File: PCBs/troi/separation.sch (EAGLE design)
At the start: 2 parts

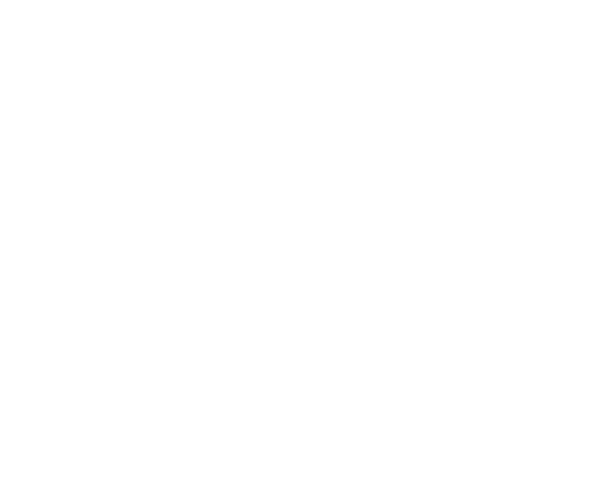
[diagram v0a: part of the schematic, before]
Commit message: added servo connection
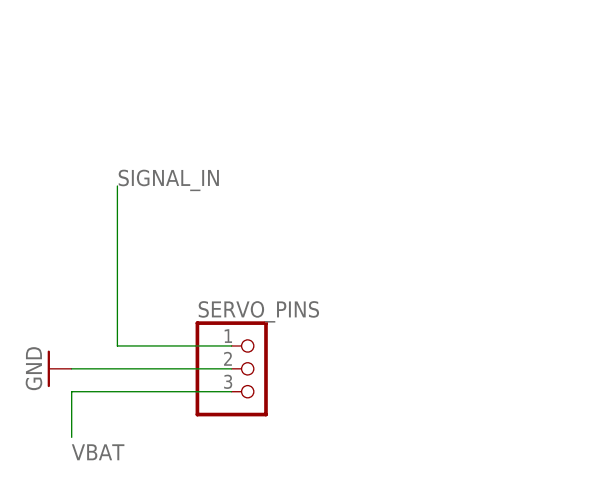
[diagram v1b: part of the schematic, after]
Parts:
- added SERVO_PINS: (no value), pinhead:PINHD-1X3
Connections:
- new net SIGNAL_IN: SERVO_PINS.1
- new net VBAT: SERVO_PINS.3
- net GND: now also SERVO_PINS.2
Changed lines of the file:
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@@
 <part name="+3V1" library="supply1" library_urn="urn:adsk.eagle:library:371" deviceset="+3V3" device=""/>
 <part name="GND1" library="supply1" library_urn="urn:adsk.eagle:library:371" deviceset="GND" device=""/>
+<part name="SERVO_PINS" library="pinhead" library_urn="urn:adsk.eagle:library:325" deviceset="PINHD-1X3" device="" package3d_urn="urn:adsk.eagle:package:22458/2"/>
+<part name="GND2" library="supply1" library_urn="urn:adsk.eagle:library:371" deviceset="GND" device=""/>
 </parts>
 <sheets>
@@
 <instance part="GND1" gate="1" x="93.98" y="86.36" smashed="yes" rot="R270">
 <attribute name="VALUE" x="86.36" y="86.36" size="1.778" layer="96"/>
+</instance>
+<instance part="SERVO_PINS" gate="A" x="30.48" y="53.34" smashed="yes">
+<attribute name="NAME" x="24.13" y="59.055" size="1.778" layer="95"/>
+<attribute name="VALUE" x="24.13" y="45.72" size="1.778" layer="96"/>
+</instance>
+<instance part="GND2" gate="1" x="7.62" y="53.34" smashed="yes" rot="R270">
+<attribute name="VALUE" x="5.08" y="55.88" size="1.778" layer="96" rot="R270"/>
 </instance>
 </instances>
@@
 <pinref part="GND1" gate="1" pin="GND"/>
 </segment>
+<segment>
+<pinref part="SERVO_PINS" gate="A" pin="2"/>
+<wire x1="27.94" y1="53.34" x2="10.16" y2="53.34" width="0.1524" layer="91"/>
+<pinref part="GND2" gate="1" pin="GND"/>
+</segment>
 </net>
 <net name="+3V3" class="0">
@@
 </segment>
 </net>
+<net name="SIGNAL_IN" class="0">
+<segment>
+<pinref part="SERVO_PINS" gate="A" pin="1"/>
+<wire x1="27.94" y1="55.88" x2="15.24" y2="55.88" width="0.1524" layer="91"/>
+<wire x1="15.24" y1="55.88" x2="15.24" y2="73.66" width="0.1524" layer="91"/>
+<label x="15.24" y="73.66" size="1.778" layer="95"/>
+</segment>
+</net>
+<net name="VBAT" class="0">
+<segment>
+<pinref part="SERVO_PINS" gate="A" pin="3"/>
+<wire x1="27.94" y1="50.8" x2="10.16" y2="50.8" width="0.1524" layer="91"/>
+<wire x1="10.16" y1="50.8" x2="10.16" y2="45.72" width="0.1524" layer="91"/>
+<label x="10.16" y="43.18" size="1.778" layer="95"/>
+</segment>
+</net>

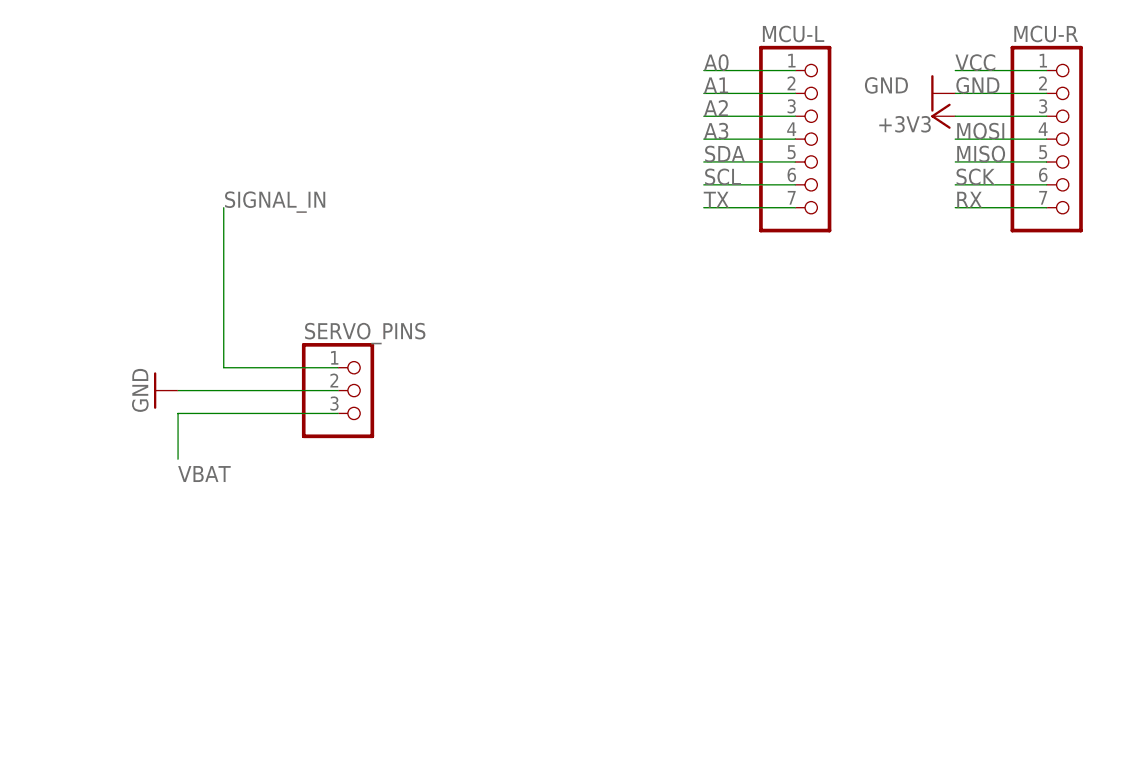
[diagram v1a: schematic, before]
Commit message: added battery terminal
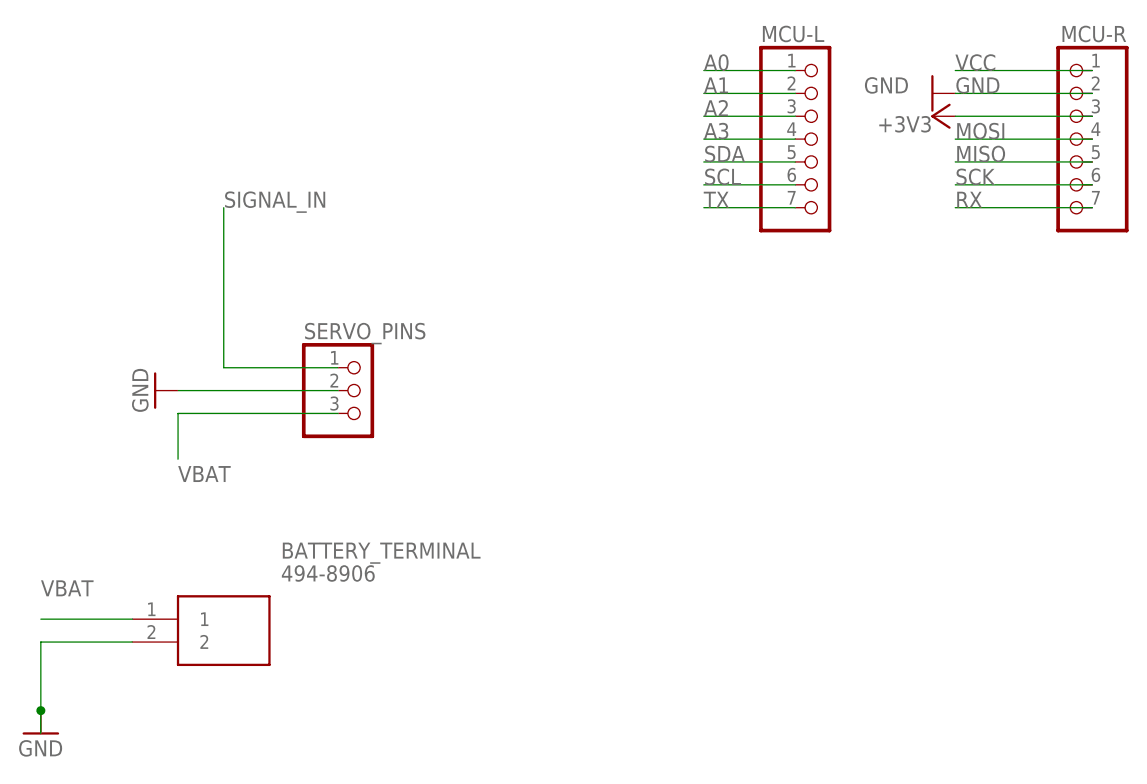
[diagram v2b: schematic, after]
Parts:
- added BATTERY_TERMINAL: 494-8906, 494-8906:494-8906
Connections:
- net GND: now also BATTERY_TERMINAL.2
- net VBAT: now also BATTERY_TERMINAL.1
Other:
- moved on the sheet: MCU-R
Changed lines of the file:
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@@
 <part name="SERVO_PINS" library="pinhead" library_urn="urn:adsk.eagle:library:325" deviceset="PINHD-1X3" device="" package3d_urn="urn:adsk.eagle:package:22458/2"/>
 <part name="GND2" library="supply1" library_urn="urn:adsk.eagle:library:371" deviceset="GND" device=""/>
+<part name="BATTERY_TERMINAL" library="494-8906" deviceset="494-8906" device=""/>
+<part name="GND3" library="supply1" library_urn="urn:adsk.eagle:library:371" deviceset="GND" device=""/>
 </parts>
 <sheets>
@@
 <attribute name="VALUE" x="74.93" y="68.58" size="1.778" layer="96"/>
 </instance>
-<instance part="MCU-R" gate="A" x="109.22" y="81.28" smashed="yes">
-<attribute name="NAME" x="102.87" y="92.075" size="1.778" layer="95"/>
-<attribute name="VALUE" x="102.87" y="68.58" size="1.778" layer="96"/>
+<instance part="MCU-R" gate="A" x="109.22" y="81.28" smashed="yes" rot="MR0">
+<attribute name="NAME" x="115.57" y="92.075" size="1.778" layer="95" rot="MR0"/>
+<attribute name="VALUE" x="115.57" y="68.58" size="1.778" layer="96" rot="MR0"/>
 </instance>
 <instance part="+3V1" gate="G$1" x="93.98" y="83.82" smashed="yes" rot="R90">
@@
 <instance part="GND2" gate="1" x="7.62" y="53.34" smashed="yes" rot="R270">
 <attribute name="VALUE" x="5.08" y="55.88" size="1.778" layer="96" rot="R270"/>
+</instance>
+<instance part="BATTERY_TERMINAL" gate="G$1" x="5.08" y="27.94" smashed="yes">
+<attribute name="NAME" x="21.59" y="35.56" size="1.778" layer="95" align="center-left"/>
+<attribute name="VALUE" x="21.59" y="33.02" size="1.778" layer="96" align="center-left"/>
+</instance>
+<instance part="GND3" gate="1" x="-5.08" y="15.24" smashed="yes">
+<attribute name="VALUE" x="-7.62" y="12.7" size="1.778" layer="96"/>
 </instance>
 </instances>
@@
 <segment>
 <pinref part="MCU-R" gate="A" pin="1"/>
-<wire x1="106.68" y1="88.9" x2="96.52" y2="88.9" width="0.1524" layer="91"/>
+<wire x1="111.76" y1="88.9" x2="96.52" y2="88.9" width="0.1524" layer="91"/>
 <label x="96.52" y="88.9" size="1.778" layer="95"/>
 </segment>
@@
 <segment>
 <pinref part="MCU-R" gate="A" pin="2"/>
-<wire x1="106.68" y1="86.36" x2="96.52" y2="86.36" width="0.1524" layer="91"/>
+<wire x1="111.76" y1="86.36" x2="96.52" y2="86.36" width="0.1524" layer="91"/>
 <label x="96.52" y="86.36" size="1.778" layer="95"/>
 <pinref part="GND1" gate="1" pin="GND"/>
@@
 <pinref part="GND2" gate="1" pin="GND"/>
 </segment>
+<segment>
+<pinref part="BATTERY_TERMINAL" gate="G$1" pin="2"/>
+<wire x1="5.08" y1="25.4" x2="-5.08" y2="25.4" width="0.1524" layer="91"/>
+<wire x1="-5.08" y1="25.4" x2="-5.08" y2="17.78" width="0.1524" layer="91"/>
+<pinref part="GND3" gate="1" pin="GND"/>
+<wire x1="-5.08" y1="17.78" x2="-5.08" y2="15.24" width="0.1524" layer="91"/>
+<junction x="-5.08" y="17.78"/>
+</segment>
 </net>
 <net name="+3V3" class="0">
 <segment>
 <pinref part="MCU-R" gate="A" pin="3"/>
-<wire x1="106.68" y1="83.82" x2="96.52" y2="83.82" width="0.1524" layer="91"/>
+<wire x1="111.76" y1="83.82" x2="96.52" y2="83.82" width="0.1524" layer="91"/>
 <pinref part="+3V1" gate="G$1" pin="+3V3"/>
 </segment>
@@
 <segment>
 <pinref part="MCU-R" gate="A" pin="4"/>
-<wire x1="106.68" y1="81.28" x2="96.52" y2="81.28" width="0.1524" layer="91"/>
+<wire x1="111.76" y1="81.28" x2="96.52" y2="81.28" width="0.1524" layer="91"/>
 <label x="96.52" y="81.28" size="1.778" layer="95"/>
 </segment>
@@
 <segment>
 <pinref part="MCU-R" gate="A" pin="5"/>
-<wire x1="106.68" y1="78.74" x2="96.52" y2="78.74" width="0.1524" layer="91"/>
+<wire x1="111.76" y1="78.74" x2="96.52" y2="78.74" width="0.1524" layer="91"/>
 <label x="96.52" y="78.74" size="1.778" layer="95"/>
 </segment>
@@
 <segment>
 <pinref part="MCU-R" gate="A" pin="6"/>
-<wire x1="106.68" y1="76.2" x2="96.52" y2="76.2" width="0.1524" layer="91"/>
+<wire x1="111.76" y1="76.2" x2="96.52" y2="76.2" width="0.1524" layer="91"/>
 <label x="96.52" y="76.2" size="1.778" layer="95"/>
 </segment>
@@
 <segment>
 <pinref part="MCU-R" gate="A" pin="7"/>
-<wire x1="106.68" y1="73.66" x2="96.52" y2="73.66" width="0.1524" layer="91"/>
+<wire x1="111.76" y1="73.66" x2="96.52" y2="73.66" width="0.1524" layer="91"/>
 <label x="96.52" y="73.66" size="1.778" layer="95"/>
 </segment>
@@
 <label x="10.16" y="43.18" size="1.778" layer="95"/>
 </segment>
+<segment>
+<pinref part="BATTERY_TERMINAL" gate="G$1" pin="1"/>
+<wire x1="5.08" y1="27.94" x2="-5.08" y2="27.94" width="0.1524" layer="91"/>
+<label x="-5.08" y="30.48" size="1.778" layer="95"/>
+</segment>
 </net>
